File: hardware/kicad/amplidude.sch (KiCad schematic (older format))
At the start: 25 parts

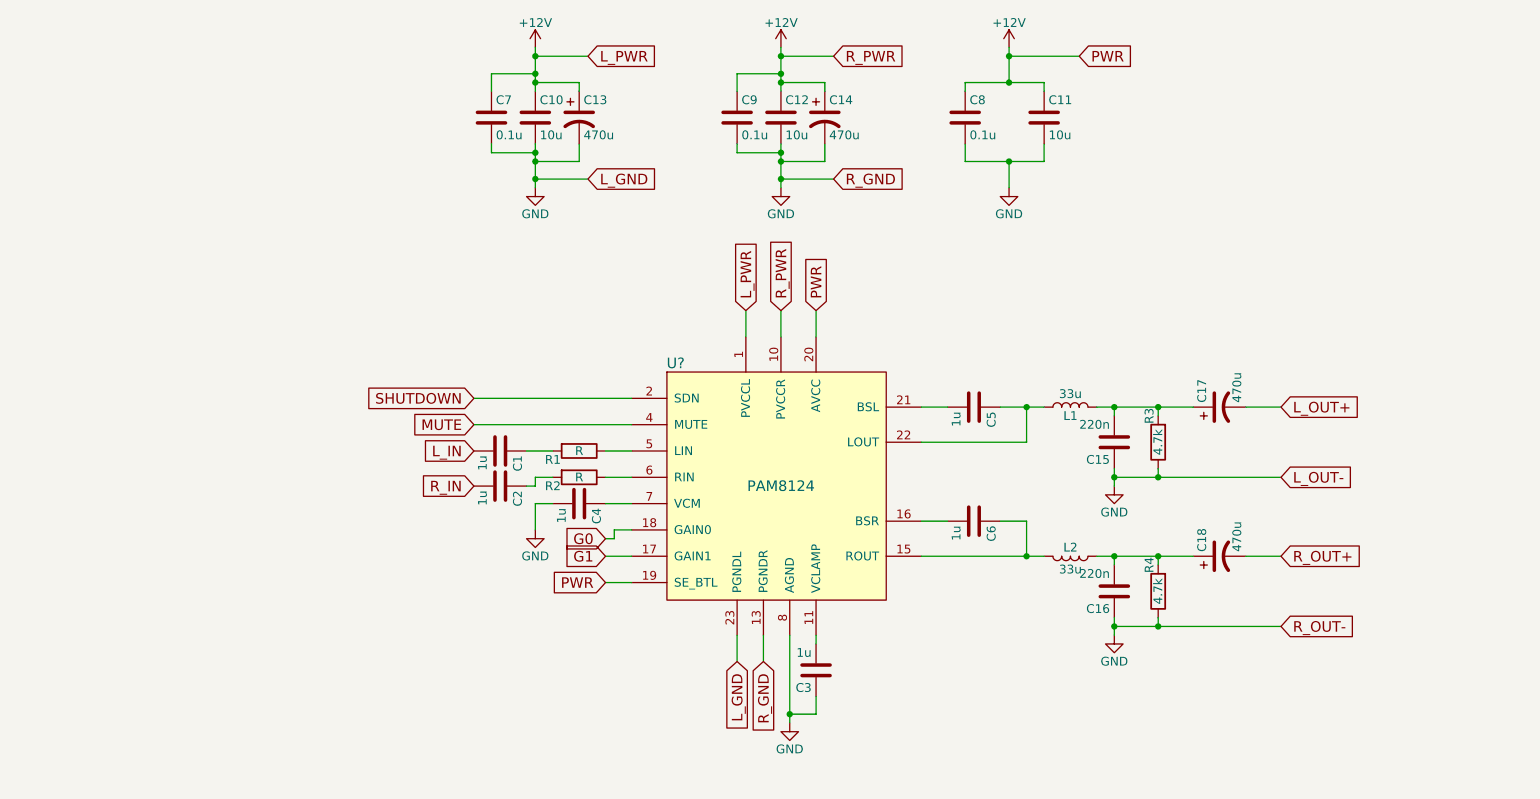
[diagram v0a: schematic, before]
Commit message: Move some overlapping components
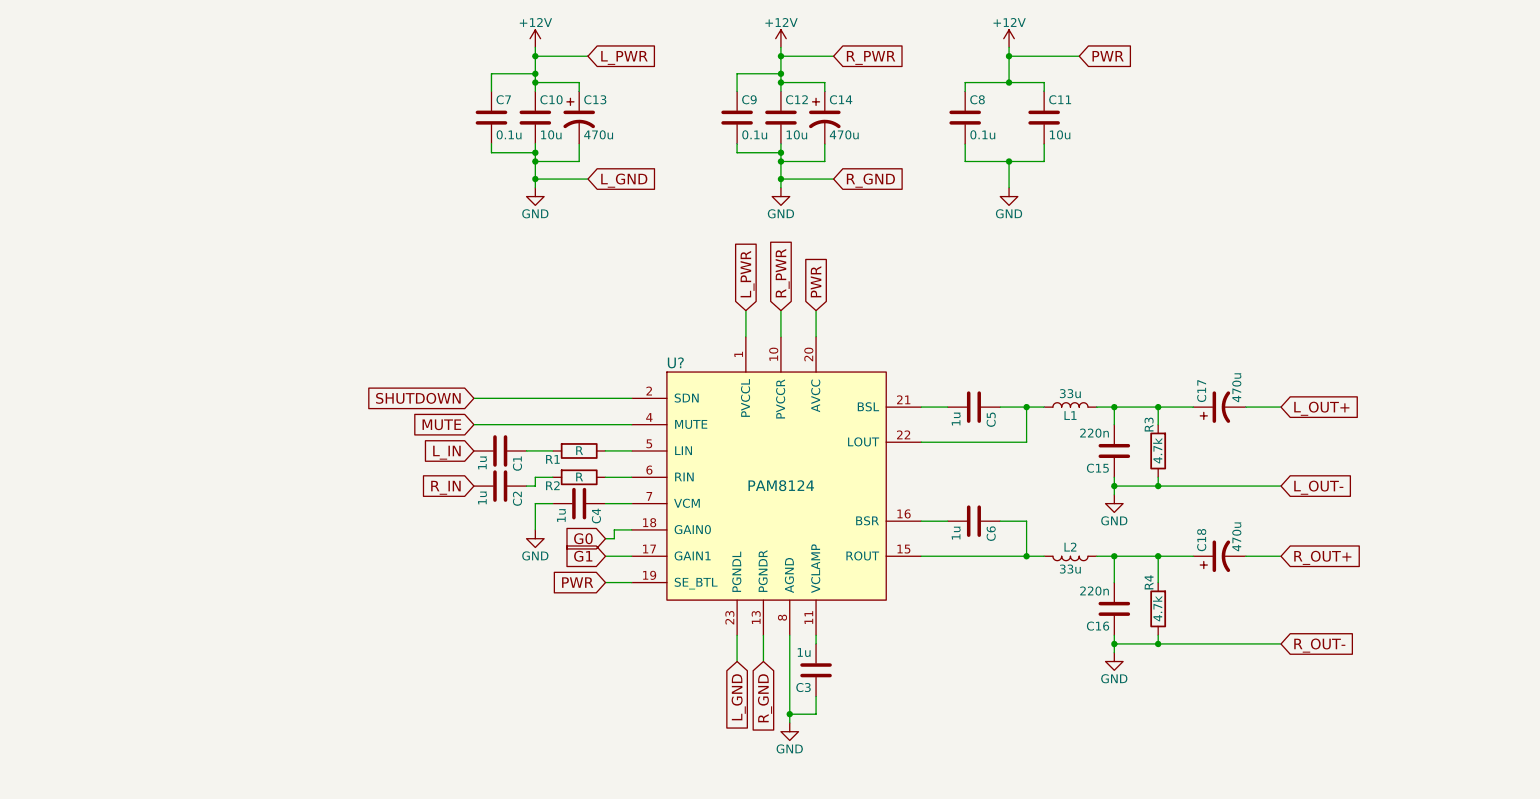
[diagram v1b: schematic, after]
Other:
- moved on the sheet: C15, C16, R3, R4
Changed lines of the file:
@@
 $EndComp
 Wire Wire Line
-	5400 4950 5400 5450
+	5400 4950 5400 5400
+Wire Wire Line
+	5400 5400 5400 5450
 $Comp
 L GND #PWR?
@@
 	6150 4300 6300 4300
 Wire Wire Line
-	6150 4500 6850 4500
+	6150 4500 6750 4500
+Wire Wire Line
+	6750 4500 6850 4500
 Wire Wire Line
 	6150 3650 6300 3650
@@
 Connection ~ 6750 4500
 Wire Wire Line
-	6600 3650 6850 3650
+	6600 3650 6750 3650
+Wire Wire Line
+	6750 3650 6850 3650
 $Comp
 L C C15
 U 1 1 596B0A5F
-P 7250 3850
-F 0 "C15" H 7275 3950 50  0000 L CNN
-F 1 "220n" H 7275 3750 50  0000 L CNN
-F 2 "" H 7288 3700 50  0001 C CNN
-F 3 "" H 7250 3850 50  0001 C CNN
-	1    7250 3850
+P 7250 3900
+F 0 "C15" H 7275 4000 50  0000 L CNN
+F 1 "220n" H 7275 3800 50  0000 L CNN
+F 2 "" H 7288 3750 50  0001 C CNN
+F 3 "" H 7250 3900 50  0001 C CNN
+	1    7250 3900
 	-1   0    0    1
 $EndComp
@@
 L C C16
 U 1 1 596B0AB9
-P 7250 4700
-F 0 "C16" H 7275 4800 50  0000 L CNN
-F 1 "220n" H 7275 4600 50  0000 L CNN
-F 2 "" H 7288 4550 50  0001 C CNN
-F 3 "" H 7250 4700 50  0001 C CNN
-	1    7250 4700
+P 7250 4800
+F 0 "C16" H 7275 4900 50  0000 L CNN
+F 1 "220n" H 7275 4700 50  0000 L CNN
+F 2 "" H 7288 4650 50  0001 C CNN
+F 3 "" H 7250 4800 50  0001 C CNN
+	1    7250 4800
 	-1   0    0    1
 $EndComp
 Wire Wire Line
-	7150 4500 7700 4500
-Wire Wire Line
-	7250 4500 7250 4550
-Wire Wire Line
-	7150 3650 7700 3650
-Wire Wire Line
-	7250 3650 7250 3700
+	7150 4500 7250 4500
+Wire Wire Line
+	7250 4500 7500 4500
+Wire Wire Line
+	7500 4500 7700 4500
+Wire Wire Line
+	7250 4500 7250 4650
+Wire Wire Line
+	7150 3650 7250 3650
+Wire Wire Line
+	7250 3650 7500 3650
+Wire Wire Line
+	7500 3650 7700 3650
+Wire Wire Line
+	7250 3650 7250 3750
 $Comp
 L GND #PWR?
 U 1 1 596B0BF2
-P 7250 4950
-F 0 "#PWR?" H 7250 4700 50  0001 C CNN
-F 1 "GND" H 7250 4800 50  0000 C CNN
-F 2 "" H 7250 4950 50  0001 C CNN
-F 3 "" H 7250 4950 50  0001 C CNN
-	1    7250 4950
-	1    0    0    -1
-$EndComp
-Wire Wire Line
-	7250 4850 7250 4950
-Wire Wire Line
-	7250 4000 7250 4100
+P 7250 5050
+F 0 "#PWR?" H 7250 4800 50  0001 C CNN
+F 1 "GND" H 7250 4900 50  0000 C CNN
+F 2 "" H 7250 5050 50  0001 C CNN
+F 3 "" H 7250 5050 50  0001 C CNN
+	1    7250 5050
+	1    0    0    -1
+$EndComp
+Wire Wire Line
+	7250 4950 7250 5000
+Wire Wire Line
+	7250 5000 7250 5050
+Wire Wire Line
+	7250 4050 7250 4100
+Wire Wire Line
+	7250 4100 7250 4150
 $Comp
 L R R3
 U 1 1 596B0CDA
-P 7500 3850
-F 0 "R3" V 7550 3700 50  0000 C CNN
-F 1 "4.7k" V 7500 3850 50  0000 C CNN
-F 2 "" V 7430 3850 50  0001 C CNN
-F 3 "" H 7500 3850 50  0001 C CNN
-	1    7500 3850
+P 7500 3900
+F 0 "R3" V 7550 3750 50  0000 C CNN
+F 1 "4.7k" V 7500 3900 50  0000 C CNN
+F 2 "" V 7430 3900 50  0001 C CNN
+F 3 "" H 7500 3900 50  0001 C CNN
+	1    7500 3900
 	-1   0    0    1
 $EndComp
@@
 L R R4
 U 1 1 596B0D3C
-P 7500 4700
-F 0 "R4" V 7550 4550 50  0000 C CNN
-F 1 "4.7k" V 7500 4700 50  0000 C CNN
-F 2 "" V 7430 4700 50  0001 C CNN
-F 3 "" H 7500 4700 50  0001 C CNN
-	1    7500 4700
+P 7500 4800
+F 0 "R4" V 7550 4650 50  0000 C CNN
+F 1 "4.7k" V 7500 4800 50  0000 C CNN
+F 2 "" V 7430 4800 50  0001 C CNN
+F 3 "" H 7500 4800 50  0001 C CNN
+	1    7500 4800
 	-1   0    0    1
 $EndComp
 Wire Wire Line
-	7500 4500 7500 4550
+	7500 4500 7500 4650
 Connection ~ 7250 4500
 Wire Wire Line
-	7500 4850 7500 4900
-Wire Wire Line
-	7500 3650 7500 3700
+	7500 4950 7500 5000
+Wire Wire Line
+	7500 3650 7500 3750
 Connection ~ 7250 3650
 Wire Wire Line
-	7500 4000 7500 4050
-Wire Wire Line
-	7250 4050 8200 4050
+	7500 4050 7500 4100
+Wire Wire Line
+	7250 4100 7500 4100
+Wire Wire Line
+	7500 4100 8200 4100
 $Comp
 L CP1 C17
@@
 Text GLabel 8200 3650 2    60   Input ~ 0
 L_OUT+
-Text GLabel 8200 4050 2    60   Input ~ 0
+Text GLabel 8200 4100 2    60   Input ~ 0
 L_OUT-
 Text GLabel 8200 4500 2    60   Input ~ 0
 R_OUT+
-Text GLabel 8200 4900 2    60   Input ~ 0
+Text GLabel 8200 5000 2    60   Input ~ 0
 R_OUT-
 Wire Wire Line
 	8200 4500 8000 4500
-Connection ~ 7500 4900
+Connection ~ 7500 5000
 Wire Wire Line
 	8200 3650 8000 3650
-Connection ~ 7500 4050
+Connection ~ 7500 4100
 Wire Wire Line
 	6150 3850 6750 3850
@@
 L GND #PWR?
 U 1 1 596B0C50
-P 7250 4100
-F 0 "#PWR?" H 7250 3850 50  0001 C CNN
-F 1 "GND" H 7250 3950 50  0000 C CNN
-F 2 "" H 7250 4100 50  0001 C CNN
-F 3 "" H 7250 4100 50  0001 C CNN
-	1    7250 4100
-	1    0    0    -1
-$EndComp
-Connection ~ 7250 4050
-Wire Wire Line
-	7250 4900 8200 4900
-Connection ~ 7250 4900
+P 7250 4150
+F 0 "#PWR?" H 7250 3900 50  0001 C CNN
+F 1 "GND" H 7250 4000 50  0000 C CNN
+F 2 "" H 7250 4150 50  0001 C CNN
+F 3 "" H 7250 4150 50  0001 C CNN
+	1    7250 4150
+	1    0    0    -1
+$EndComp
+Connection ~ 7250 4100
+Wire Wire Line
+	7250 5000 7500 5000
+Wire Wire Line
+	7500 5000 8200 5000
+Connection ~ 7250 5000
 Text GLabel 4350 4400 0    60   Input ~ 0
 G0
@@
 $EndComp
 Wire Wire Line
-	3950 2150 3950 2400
+	3950 2150 3950 2200
+Wire Wire Line
+	3950 2200 3950 2250
+Wire Wire Line
+	3950 2250 3950 2350
+Wire Wire Line
+	3950 2350 3950 2400
 Wire Wire Line
 	4200 2150 4200 2250
@@
 Connection ~ 3950 2200
 Wire Wire Line
-	3950 1600 3950 1850
+	3950 1600 3950 1650
+Wire Wire Line
+	3950 1650 3950 1750
+Wire Wire Line
+	3950 1750 3950 1800
+Wire Wire Line
+	3950 1800 3950 1850
 Wire Wire Line
 	3700 1850 3700 1750
@@
 $EndComp
 Wire Wire Line
-	5350 2150 5350 2400
+	5350 2150 5350 2200
+Wire Wire Line
+	5350 2200 5350 2250
+Wire Wire Line
+	5350 2250 5350 2350
+Wire Wire Line
+	5350 2350 5350 2400
 Wire Wire Line
 	5600 2150 5600 2250
@@
 Connection ~ 5350 2200
 Wire Wire Line
-	5350 1600 5350 1850
+	5350 1600 5350 1650
+Wire Wire Line
+	5350 1650 5350 1750
+Wire Wire Line
+	5350 1750 5350 1800
+Wire Wire Line
+	5350 1800 5350 1850
 Wire Wire Line
 	5100 1850 5100 1750
@@
 $EndComp
 Wire Wire Line
-	6650 1600 6650 1800
-Wire Wire Line
-	6400 1800 6850 1800
+	6650 1600 6650 1650
+Wire Wire Line
+	6650 1650 6650 1800
+Wire Wire Line
+	6400 1800 6650 1800
+Wire Wire Line
+	6650 1800 6850 1800
 Wire Wire Line
 	6400 1800 6400 1850
@@
 	6400 2150 6400 2250
 Wire Wire Line
-	6400 2250 6850 2250
+	6400 2250 6650 2250
+Wire Wire Line
+	6650 2250 6850 2250
 Wire Wire Line
 	6650 2250 6650 2400

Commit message: Add some connectors for in/out and shutdown/mute
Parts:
- added J? (x4): CONN_01X02_MALE, symbol CONN_01X02_MALE
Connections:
- net AGND: now also J?.2, J?.2
- net L_IN: now also J?.1
- net L_OUT+: now also J?.1
- net MUTE: now also J?.2
- net R_IN: now also J?.2
- net R_OUT+: now also J?.1
- net SHUTDOWN: now also J?.1
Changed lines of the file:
@@
 $EndComp
 Wire Wire Line
-	5400 4950 5400 5400
-Wire Wire Line
-	5400 5400 5400 5450
+	5400 4950 5400 5450
 $Comp
 L GND #PWR?
@@
 Wire Wire Line
 	3950 4100 3900 4100
-Text GLabel 3600 3900 0    60   Input ~ 0
-L_IN
-Text GLabel 3600 4100 0    60   Input ~ 0
-R_IN
-Text GLabel 3600 3750 0    60   Input ~ 0
-MUTE
-Wire Wire Line
-	3600 3750 4500 3750
+Wire Wire Line
+	2750 3750 4500 3750
 $Comp
 L C C3
@@
 	6150 4300 6300 4300
 Wire Wire Line
-	6150 4500 6750 4500
-Wire Wire Line
-	6750 4500 6850 4500
+	6150 4500 6850 4500
 Wire Wire Line
 	6150 3650 6300 3650
@@
 Connection ~ 6750 4500
 Wire Wire Line
-	6600 3650 6750 3650
-Wire Wire Line
-	6750 3650 6850 3650
+	6600 3650 6850 3650
 $Comp
 L C C15
@@
 $EndComp
 Wire Wire Line
-	7150 4500 7250 4500
-Wire Wire Line
-	7250 4500 7500 4500
-Wire Wire Line
-	7500 4500 7700 4500
+	7150 4500 7700 4500
 Wire Wire Line
 	7250 4500 7250 4650
 Wire Wire Line
-	7150 3650 7250 3650
-Wire Wire Line
-	7250 3650 7500 3650
-Wire Wire Line
-	7500 3650 7700 3650
+	7150 3650 7700 3650
 Wire Wire Line
 	7250 3650 7250 3750
@@
 $EndComp
 Wire Wire Line
-	7250 4950 7250 5000
-Wire Wire Line
-	7250 5000 7250 5050
-Wire Wire Line
-	7250 4050 7250 4100
-Wire Wire Line
-	7250 4100 7250 4150
+	7250 4950 7250 5050
+Wire Wire Line
+	7250 4050 7250 4150
 $Comp
 L R R3
@@
 	7500 4050 7500 4100
 Wire Wire Line
-	7250 4100 7500 4100
-Wire Wire Line
-	7500 4100 8200 4100
+	7250 4100 8200 4100
 $Comp
 L CP1 C17
@@
 Connection ~ 7500 3650
 Connection ~ 7500 4500
-Text GLabel 8200 3650 2    60   Input ~ 0
-L_OUT+
-Text GLabel 8200 4100 2    60   Input ~ 0
-L_OUT-
-Text GLabel 8200 4500 2    60   Input ~ 0
-R_OUT+
-Text GLabel 8200 5000 2    60   Input ~ 0
-R_OUT-
 Wire Wire Line
 	8200 4500 8000 4500
@@
 Connection ~ 7250 4100
 Wire Wire Line
-	7250 5000 7500 5000
-Wire Wire Line
-	7500 5000 8200 5000
+	7250 5000 8200 5000
 Connection ~ 7250 5000
 Text GLabel 4350 4400 0    60   Input ~ 0
@@
 Wire Wire Line
 	5100 5100 5100 4950
-Text GLabel 3600 3600 0    60   Input ~ 0
-SHUTDOWN
-Wire Wire Line
-	3600 3600 4500 3600
+Wire Wire Line
+	2650 3600 4500 3600
 $Comp
 L +12V #PWR?
@@
 $EndComp
 Wire Wire Line
-	3950 2150 3950 2200
-Wire Wire Line
-	3950 2200 3950 2250
-Wire Wire Line
-	3950 2250 3950 2350
-Wire Wire Line
-	3950 2350 3950 2400
+	3950 2150 3950 2400
 Wire Wire Line
 	4200 2150 4200 2250
@@
 Connection ~ 3950 2200
 Wire Wire Line
-	3950 1600 3950 1650
-Wire Wire Line
-	3950 1650 3950 1750
-Wire Wire Line
-	3950 1750 3950 1800
-Wire Wire Line
-	3950 1800 3950 1850
+	3950 1600 3950 1850
 Wire Wire Line
 	3700 1850 3700 1750
@@
 $EndComp
 Wire Wire Line
-	5350 2150 5350 2200
-Wire Wire Line
-	5350 2200 5350 2250
-Wire Wire Line
-	5350 2250 5350 2350
-Wire Wire Line
-	5350 2350 5350 2400
+	5350 2150 5350 2400
 Wire Wire Line
 	5600 2150 5600 2250
@@
 Connection ~ 5350 2200
 Wire Wire Line
-	5350 1600 5350 1650
-Wire Wire Line
-	5350 1650 5350 1750
-Wire Wire Line
-	5350 1750 5350 1800
-Wire Wire Line
-	5350 1800 5350 1850
+	5350 1600 5350 1850
 Wire Wire Line
 	5100 1850 5100 1750
@@
 $EndComp
 Wire Wire Line
-	6650 1600 6650 1650
-Wire Wire Line
-	6650 1650 6650 1800
-Wire Wire Line
-	6400 1800 6650 1800
-Wire Wire Line
-	6650 1800 6850 1800
+	6650 1600 6650 1800
+Wire Wire Line
+	6400 1800 6850 1800
 Wire Wire Line
 	6400 1800 6400 1850
@@
 	6400 2150 6400 2250
 Wire Wire Line
-	6400 2250 6650 2250
-Wire Wire Line
-	6650 2250 6850 2250
+	6400 2250 6850 2250
 Wire Wire Line
 	6650 2250 6650 2400
@@
 	7050 1650 6650 1650
 Connection ~ 6650 1650
+$Comp
+L CONN_01X02_MALE J?
+U 1 1 596BDC3A
+P 2950 4000
+F 0 "J?" H 2950 4175 50  0000 C CNN
+F 1 "CONN_01X02_MALE" H 2950 3800 50  0000 C CNN
+F 2 "" H 2950 4100 50  0001 C CNN
+F 3 "" H 2950 4100 50  0001 C CNN
+	1    2950 4000
+	1    0    0    -1
+$EndComp
+Wire Wire Line
+	3250 3900 3600 3900
+Wire Wire Line
+	3250 4100 3600 4100
+Text Label 3300 3900 0    60   ~ 0
+L_IN
+Text Label 3300 4100 0    60   ~ 0
+R_IN
+$Comp
+L CONN_01X02_MALE J?
+U 1 1 596BE036
+P 2350 3700
+F 0 "J?" H 2350 3875 50  0000 C CNN
+F 1 "CONN_01X02_MALE" H 2350 3500 50  0000 C CNN
+F 2 "" H 2350 3800 50  0001 C CNN
+F 3 "" H 2350 3800 50  0001 C CNN
+	1    2350 3700
+	1    0    0    -1
+$EndComp
+Wire Wire Line
+	2750 3750 2750 3800
+Wire Wire Line
+	2750 3800 2650 3800
+Text Label 3300 3600 0    60   ~ 0
+SHUTDOWN
+Text Label 3300 3750 0    60   ~ 0
+MUTE
+$Comp
+L CONN_01X02_MALE J?
+U 1 1 596BE42C
+P 9200 3850
+F 0 "J?" H 9200 4025 50  0000 C CNN
+F 1 "CONN_01X02_MALE" H 9200 3650 50  0000 C CNN
+F 2 "" H 9200 3950 50  0001 C CNN
+F 3 "" H 9200 3950 50  0001 C CNN
+	1    9200 3850
+	-1   0    0    -1
+$EndComp
+$Comp
+L CONN_01X02_MALE J?
+U 1 1 596BE4E2
+P 9200 4750
+F 0 "J?" H 9200 4925 50  0000 C CNN
+F 1 "CONN_01X02_MALE" H 9200 4550 50  0000 C CNN
+F 2 "" H 9200 4850 50  0001 C CNN
+F 3 "" H 9200 4850 50  0001 C CNN
+	1    9200 4750
+	-1   0    0    -1
+$EndComp
+Wire Wire Line
+	8200 3650 8200 3750
+Wire Wire Line
+	8200 3750 8900 3750
+Wire Wire Line
+	8200 4100 8200 3950
+Wire Wire Line
+	8200 3950 8900 3950
+Text Label 8450 3750 0    60   ~ 0
+L_OUT+
+Text Label 8450 3950 0    60   ~ 0
+L_OUT-
+Wire Wire Line
+	8200 4500 8200 4650
+Wire Wire Line
+	8200 4650 8900 4650
+Wire Wire Line
+	8200 5000 8200 4850
+Wire Wire Line
+	8200 4850 8900 4850
+Text Label 8450 4650 0    60   ~ 0
+R_OUT+
+Text Label 8450 4850 0    60   ~ 0
+R_OUT-
 $EndSCHEMATC
